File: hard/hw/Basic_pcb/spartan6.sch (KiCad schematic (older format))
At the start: 52 parts, among them IC1 MT48LC4M16A2P, J1 HDMI_A, X1 OSCILLATORS-1

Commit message: Actualizacion Power
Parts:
- removed CF30, CF32, CF34, CF35: 33uF, opendous:SM1206_Opendous, symbol C
- removed CF31, CF33: 100n, opendous:SM0603, symbol C
- removed UF2: ZLDO1117G12TA, SMD_Packages:SOT-223, symbol LT1117CST
- removed UF3: ZLDO1117G33TA, SMD_Packages:SOT-223, symbol LT1117CST
- added R10, R11, R4, R5, R6, R7, R8, R9: 51, Resistors_SMD:R_0805, symbol R
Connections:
- net labels added: TMDS_CLK_N, TMDS_CLK_P, TMDS_D0_N, TMDS_D0_P, TMDS_D1_N, TMDS_D1_P, TMDS_D2_N, TMDS_D2_P, ~CAS, ~CS, ~RAS, ~WE
- net labels removed: CAS, CS, IO56, IO57, IO58, IO59, IO62, IO63, IO72, IO73, RAS, VDD5V, WE
- wire segments 421 -> 404
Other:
- moved on the sheet: J1

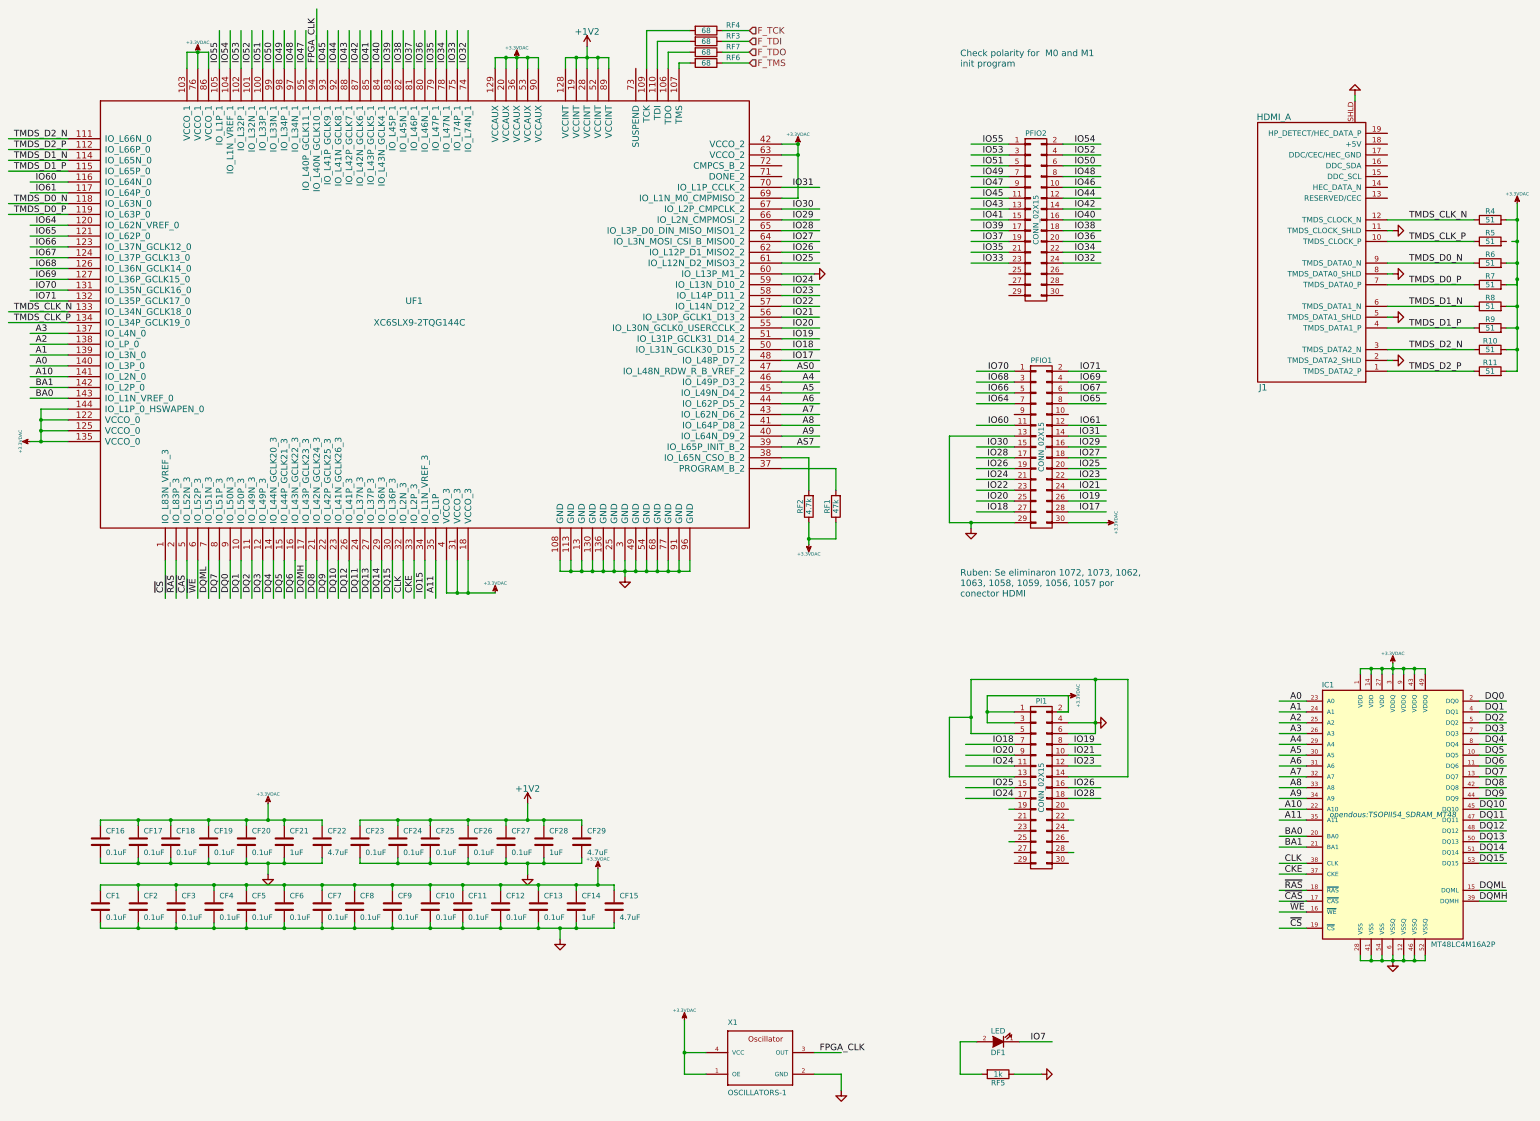
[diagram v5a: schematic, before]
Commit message: Actualización PinOut LVDS
by Rubén Parra
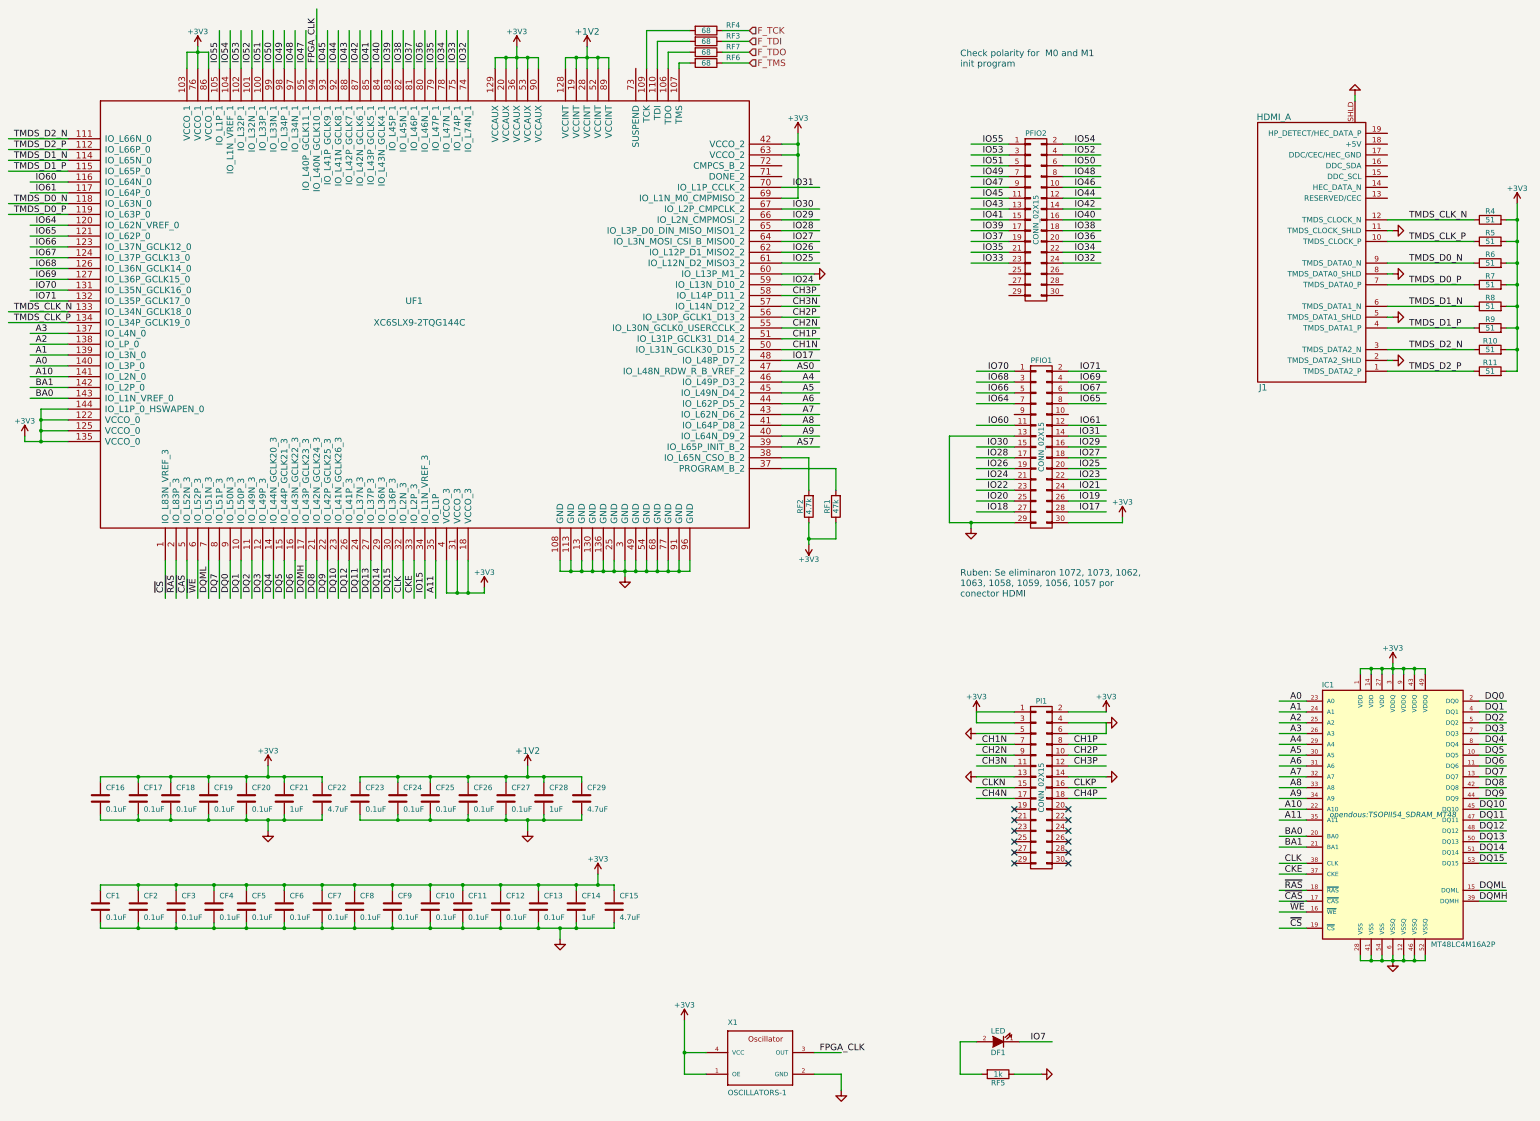
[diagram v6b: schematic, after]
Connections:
- net labels added: +3V3, CH1N, CH1P, CH2N, CH2P, CH3N, CH3P, CH4N, CH4P, CLKN, CLKP
- net labels removed: +3.3VDAC
- wire segments 404 -> 395
- no-connect marks 0 -> 12
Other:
- moved on the sheet: CF16, CF17, CF18, CF19, CF20, CF21, CF22, CF23, CF24, CF25, CF26, CF27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

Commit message: Datasheets
By Rubén
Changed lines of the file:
@@
 IO24
 Text Label 8650 2950 0    60   ~ 0
-IO25
+CLKN
 Text Label 8650 2850 0    60   ~ 0
-IO26
+CLKP
 Text Label 8650 2750 0    60   ~ 0
-IO27
+CH4N
 Text Label 8650 2650 0    60   ~ 0
-IO28
+CH4P
 Text Label 8650 2550 0    60   ~ 0
 IO29

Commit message: Actualizacion Raiz
por Rubén
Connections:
- net labels added: F_RXD, F_TXD
- net labels removed: IO18, IO19, IO20, IO21, IO22, IO23, IO25, IO26, IO27, IO28, IO52, IO55
- wire segments 395 -> 383
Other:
- note added: "Ruben: Se eliminaron 1072, 1073, 1062, \n1063, 1058, 1059, 1056, 1057 por \nconector HDMI.\nRubén: Se eliminaron IO18, IO19, \nIO20, IO21, IO22, IO23, IO25, IO26, \nIO27, IO28 por conector LVDS."
- note added: "Ruben: Se eliminaron IO55 Y IO52 \npara USB RX y TX"
- note removed: "Ruben: Se eliminaron 1072, 1073, 1062, \n1063, 1058, 1059, 1056, 1057 por \nconector HDMI"
- moved on the sheet: PFIO1, Pl1, RF1, RF2, RF3, RF4, RF6, RF7, UF1
